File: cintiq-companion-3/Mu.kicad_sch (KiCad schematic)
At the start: 12 parts, among them J1 Conn_01x03_Pin

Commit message: Made a little HSIO plan
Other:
- note added: "I got the flash image tool, so I should be able to change it to whatever I need :3"
- note added: "no actually eDP"
- note added: "rough HSIO plan: HSIO A: idk yet, many possibilities. Could add a B-key m.2 slot with PCIe and USB3 Should probably have at least one Type-A USB3 port too 0: 1: 2: 3: HSIO B: PCIe 4x1, HSIO11 sata/pcie with gpio for M-key m.2 slot 8: SSD PCIe x4 Lane 3 9: SSD PCIe x4 Lane 2 10: SSD PCIe x4 Lane 1 (/ SATA?) 11: SSD PCIe x4 Lane 0 / SATA HSIO C: PCIe 1x1 for E-key m.2 slot for Wifi 6: Wifi PCIe x1"
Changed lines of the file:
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@@
 		)
 	)
-	(text_box "DDI B used for HDMI no actually eDP\n"
+	(text_box "DDI B used for HDMI"
 		(exclude_from_sim no)
 		(at 251.46 231.14 0)
@@
 		)
 	)
-	(text "HSIO functions are defined by the BIOS source code, \nCannot be changed in BIOS settings.\n\nBefore starting design, you should choose one of\nthe available BIOS configurations on:\nhttps://github.com/LattePandaTeam/LattePanda-Mu\nOr contact techsupport for custom your BIOS\n\nThe default functions are defined as follows:\n\n- HSIO0: USB3.2 10Gbps\n- HSIO1: USB3.2 10Gbps\n- HSIO2: PCIe 3.0 x1\n- HSIO3: PCIe 3.0 x1\n\n- HSIO8: PCIe 3.0 x4 (Lane 0)\n- HSIO9: PCIe 3.0 x4 (Lane 1)\n- HSIO10: PCIe 3.0 x4 (Lane 2)\n- HSIO11: PCIe 3.0 x4 (Lane 3)\n\n- HSIO6: PCIe 3.0 x1"
+	(text "HSIO functions are defined by the BIOS source code, \nCannot be changed in BIOS settings.\n\nBefore starting design, you should choose one of\nthe available BIOS configurations on:\nhttps://github.com/LattePandaTeam/LattePanda-Mu\nOr contact techsupport for custom your BIOS\n\nThe default functions are defined as follows:\n\n- HSIO0: USB3.2 10Gbps\n- HSIO1: USB3.2 10Gbps\n- HSIO2: PCIe 3.0 x1\n- HSIO3: PCIe 3.0 x1\n\n- HSIO8: PCIe 3.0 x4 (Lane 0)\n- HSIO9: PCIe 3.0 x4 (Lane 1)\n- HSIO10: PCIe 3.0 x4 (Lane 2)\n- HSIO11: PCIe 3.0 x4 (Lane 3)\n\n- HSIO6: PCIe 3.0 x1\n"
 		(exclude_from_sim no)
-		(at 127 100.33 0)
+		(at 128.27 20.32 0)
 		(effects
 			(font
@@
 		)
 	)
+	(text "no actually eDP\n"
+		(exclude_from_sim no)
+		(at 264.16 237.49 0)
+		(effects
+			(font
+				(size 2.54 2.54)
+				(thickness 0.508)
+				(bold yes)
+				(color 255 121 154 1)
+			)
+			(justify left top)
+		)
+	)
 	(text "HPD pin of unused DDI/TCP port\nneeds to be pulled down"
 		(exclude_from_sim no)
@@
 		)
 	)
+	(text "rough HSIO plan:\n\nHSIO A:\nidk yet, many possibilities.\nCould add a B-key m.2 slot with PCIe and USB3\nShould probably have at least one Type-A USB3 port too\n0:  \n1:  \n2:  \n3:  \n\nHSIO B:\nPCIe 4x1, HSIO11 sata/pcie with gpio for M-key m.2 slot\n8:  SSD PCIe x4 Lane 3\n9:  SSD PCIe x4 Lane 2\n10: SSD PCIe x4 Lane 1 (/ SATA?)\n11: SSD PCIe x4 Lane 0 / SATA\n\nHSIO C:\nPCIe 1x1 for E-key m.2 slot for Wifi\n6:  Wifi PCIe x1 "
+		(exclude_from_sim no)
+		(at 127 123.19 0)
+		(effects
+			(font
+				(size 2.54 2.54)
+				(thickness 0.508)
+				(bold yes)
+				(color 255 121 154 1)
+			)
+			(justify left top)
+		)
+	)
 	(text "DDI/TCP functions are defined by the BIOS source code, \nCannot be changed in BIOS settings.\n\nBefore starting design, you should choose one of\nthe available BIOS configurations on:\nhttps://github.com/LattePandaTeam/LattePanda-Mu\n\nThe default functions are defined as follows:\n\n- DDIA: eDP 1.4b (the 40Pin connector on the Mu)\n\n- DDIB: HDMI 2.0\n\n- TCP0: HDMI 2.0\n\n- TCP1: USB TypeC (need external PD controller)"
 		(exclude_from_sim no)
@@
 		)
 	)
+	(text "I got the flash image tool,\nso I should be able to change\nit to whatever I need :3"
+		(exclude_from_sim no)
+		(at 128.27 107.95 0)
+		(effects
+			(font
+				(size 2.54 2.54)
+				(thickness 0.508)
+				(bold yes)
+				(color 255 121 154 1)
+			)
+			(justify left top)
+		)
+	)
 	(global_label "DDI_B_TX3+"
 		(shape output)
@@
 	)
 	(global_label "TCP0_TXRX0+"
-		(shape output)
+		(shape bidirectional)
 		(at 334.01 285.75 180)
 		(fields_autoplaced yes)
@@
 	)
 	(global_label "TCP0_TXRX1-"
-		(shape output)
+		(shape bidirectional)
 		(at 334.01 278.13 180)
 		(fields_autoplaced yes)
@@
 	)
 	(global_label "eDP_L0-"
-		(shape input)
-		(at 308.61 236.22 180)
-		(fields_autoplaced yes)
-		(effects
-			(font
-				(size 1.27 1.27)
-			)
-			(justify right)
-		)
-		(property "Intersheetrefs" "${INTERSHEET_REFS}"
-			(at 297.2186 236.22 0)
+		(shape output)
+		(at 308.61 255.27 180)
+		(fields_autoplaced yes)
+		(effects
+			(font
+				(size 1.27 1.27)
+			)
+			(justify right)
+		)
+		(property "Intersheetrefs" "${INTERSHEET_REFS}"
+			(at 297.2186 255.27 0)
 			(effects
 				(font
@@
 	)
 	(global_label "TCP1_TXRX0+"
-		(shape output)
+		(shape bidirectional)
 		(at 334.01 323.85 180)
 		(fields_autoplaced yes)
@@
 	)
 	(global_label "TCP0_TXRX0-"
-		(shape output)
+		(shape bidirectional)
 		(at 334.01 288.29 180)
 		(fields_autoplaced yes)
@@
 	)
 	(global_label "eDP_L0+"
-		(shape input)
-		(at 308.61 238.76 180)
-		(fields_autoplaced yes)
-		(effects
-			(font
-				(size 1.27 1.27)
-			)
-			(justify right)
-		)
-		(property "Intersheetrefs" "${INTERSHEET_REFS}"
-			(at 297.2186 238.76 0)
+		(shape output)
+		(at 308.61 252.73 180)
+		(fields_autoplaced yes)
+		(effects
+			(font
+				(size 1.27 1.27)
+			)
+			(justify right)
+		)
+		(property "Intersheetrefs" "${INTERSHEET_REFS}"
+			(at 297.2186 252.73 0)
 			(effects
 				(font
@@
 	)
 	(global_label "eDP_AUX-"
-		(shape input)
-		(at 308.61 246.38 180)
-		(fields_autoplaced yes)
-		(effects
-			(font
-				(size 1.27 1.27)
-			)
-			(justify right)
-		)
-		(property "Intersheetrefs" "${INTERSHEET_REFS}"
-			(at 295.8276 246.38 0)
+		(shape output)
+		(at 308.61 234.95 180)
+		(fields_autoplaced yes)
+		(effects
+			(font
+				(size 1.27 1.27)
+			)
+			(justify right)
+		)
+		(property "Intersheetrefs" "${INTERSHEET_REFS}"
+			(at 295.8276 234.95 0)
 			(effects
 				(font
@@
 	)
 	(global_label "TCP1_TXRX1+"
-		(shape output)
+		(shape bidirectional)
 		(at 334.01 313.69 180)
 		(fields_autoplaced yes)
@@
 	)
 	(global_label "eDP_L1-"
-		(shape input)
-		(at 308.61 228.6 180)
-		(fields_autoplaced yes)
-		(effects
-			(font
-				(size 1.27 1.27)
-			)
-			(justify right)
-		)
-		(property "Intersheetrefs" "${INTERSHEET_REFS}"
-			(at 297.2186 228.6 0)
+		(shape output)
+		(at 308.61 250.19 180)
+		(fields_autoplaced yes)
+		(effects
+			(font
+				(size 1.27 1.27)
+			)
+			(justify right)
+		)
+		(property "Intersheetrefs" "${INTERSHEET_REFS}"
+			(at 297.2186 250.19 0)
 			(effects
 				(font
@@
 	)
 	(global_label "eDP_L1+"
-		(shape input)
-		(at 308.61 231.14 180)
-		(fields_autoplaced yes)
-		(effects
-			(font
-				(size 1.27 1.27)
-			)
-			(justify right)
-		)
-		(property "Intersheetrefs" "${INTERSHEET_REFS}"
-			(at 297.2186 231.14 0)
+		(shape output)
+		(at 308.61 247.65 180)
+		(fields_autoplaced yes)
+		(effects
+			(font
+				(size 1.27 1.27)
+			)
+			(justify right)
+		)
+		(property "Intersheetrefs" "${INTERSHEET_REFS}"
+			(at 297.2186 247.65 0)
 			(effects
 				(font
@@
 	(global_label "eDP_HPD"
 		(shape input)
-		(at 308.61 251.46 180)
-		(fields_autoplaced yes)
-		(effects
-			(font
-				(size 1.27 1.27)
-			)
-			(justify right)
-		)
-		(property "Intersheetrefs" "${INTERSHEET_REFS}"
-			(at 297.1581 251.46 0)
+		(at 308.61 222.25 180)
+		(fields_autoplaced yes)
+		(effects
+			(font
+				(size 1.27 1.27)
+			)
+			(justify right)
+		)
+		(property "Intersheetrefs" "${INTERSHEET_REFS}"
+			(at 297.1581 222.25 0)
 			(effects
 				(font
@@
 	)
 	(global_label "TCP1_TXRX1-"
-		(shape output)
+		(shape bidirectional)
 		(at 334.01 316.23 180)
 		(fields_autoplaced yes)
@@
 	)
 	(global_label "TCP0_TXRX1+"
-		(shape output)
+		(shape bidirectional)
 		(at 334.01 275.59 180)
 		(fields_autoplaced yes)
@@
 	)
 	(global_label "TCP1_TXRX0-"
-		(shape output)
+		(shape bidirectional)
 		(at 334.01 326.39 180)
 		(fields_autoplaced yes)
@@
 	)
 	(global_label "eDP_AUX+"
-		(shape input)
-		(at 308.61 243.84 180)
-		(fields_autoplaced yes)
-		(effects
-			(font
-				(size 1.27 1.27)
-			)
-			(justify right)
-		)
-		(property "Intersheetrefs" "${INTERSHEET_REFS}"
-			(at 295.8276 243.84 0)
-			(effects
-				(font
+		(shape output)
+		(at 308.61 232.41 180)
+		(fields_autoplaced yes)
+		(effects
+			(font
+				(size 1.27 1.27)
+			)
+			(justify right)
+		)
+		(property "Intersheetrefs" "${INTERSHEET_REFS}"
+			(at 295.8276 232.41 0)
+			(effects
+				(font

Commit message: Did some footprint assignments and added reference image to pcb editor
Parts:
- A1: footprint Module_LattePanda:LattePanda_Module_H8.0mm_Horizontal -> A_my_stuff:ddr4sodimm
- H7, H8: footprint A_HDJ_Library:MountingHole_3mm_M2_Pad_TopOnly -> MountingHole:MountingHole_3mm_Pad_TopOnly
- J1: footprint A_HDJ_Library:PinHeader_1x03_P2.54mm_Vertical -> Connector_PinHeader_2.54mm:PinHeader_1x03_P2.54mm_Vertical
- R4, R5, R6, R7: footprint A_HDJ_Library:R_0402_1005Metric -> Resistor_SMD:R_0402_1005Metric
- TP2: footprint A_HDJ_Library:TestPoint_Pad_D1.5mm -> TestPoint:TestPoint_Pad_D1.5mm
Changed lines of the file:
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@@
 			)
 		)
-		(property "Footprint" "A_HDJ_Library:R_0402_1005Metric"
+		(property "Footprint" "Resistor_SMD:R_0402_1005Metric"
 			(at 278.13 258.572 90)
 			(effects
@@
 			)
 		)
-		(property "Footprint" "A_HDJ_Library:R_0402_1005Metric"
+		(property "Footprint" "Resistor_SMD:R_0402_1005Metric"
 			(at 278.13 296.672 90)
 			(effects
@@
 			)
 		)
-		(property "Footprint" "Module_LattePanda:LattePanda_Module_H8.0mm_Horizontal"
+		(property "Footprint" "A_my_stuff:ddr4sodimm"
 			(at 294.386 179.07 0)
 			(effects
@@
 			)
 		)
-		(property "Footprint" "A_HDJ_Library:MountingHole_3mm_M2_Pad_TopOnly"
+		(property "Footprint" "MountingHole:MountingHole_3mm_Pad_TopOnly"
 			(at 515.62 311.15 0)
 			(effects
@@
 			)
 		)
-		(property "Footprint" "A_HDJ_Library:R_0402_1005Metric"
+		(property "Footprint" "Resistor_SMD:R_0402_1005Metric"
 			(at 412.75 57.658 90)
 			(effects
@@
 			)
 		)
-		(property "Footprint" "A_HDJ_Library:R_0402_1005Metric"
+		(property "Footprint" "Resistor_SMD:R_0402_1005Metric"
 			(at 438.15 269.748 90)
 			(effects
@@
 			)
 		)
-		(property "Footprint" "A_HDJ_Library:TestPoint_Pad_D1.5mm"
+		(property "Footprint" "TestPoint:TestPoint_Pad_D1.5mm"
 			(at 436.88 267.97 0)
 			(effects
@@
 			)
 		)
-		(property "Footprint" "A_HDJ_Library:MountingHole_3mm_M2_Pad_TopOnly"
+		(property "Footprint" "MountingHole:MountingHole_3mm_Pad_TopOnly"
 			(at 490.22 311.15 0)
 			(effects
@@
 			)
 		)
-		(property "Footprint" "A_HDJ_Library:PinHeader_1x03_P2.54mm_Vertical"
+		(property "Footprint" "Connector_PinHeader_2.54mm:PinHeader_1x03_P2.54mm_Vertical"
 			(at 292.1 74.93 0)
 			(effects

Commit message: Redid board outline according to reference and placed compute module slot
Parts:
- A1: footprint A_my_stuff:ddr4sodimm -> A_my_stuff:LattepandaMuFlat
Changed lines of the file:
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@@
 			)
 		)
-		(property "Footprint" "A_my_stuff:ddr4sodimm"
+		(property "Footprint" "A_my_stuff:LattepandaMuFlat"
 			(at 294.386 179.07 0)
 			(effects

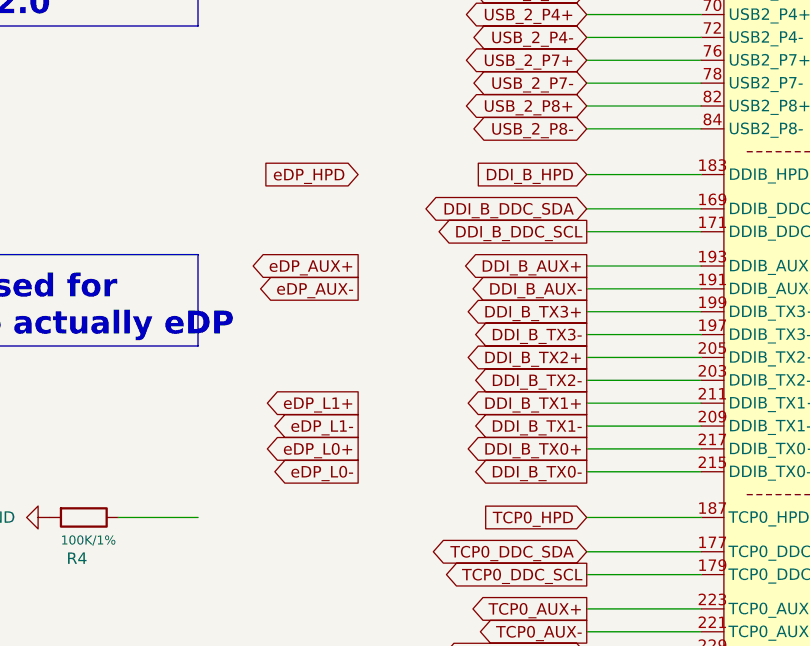
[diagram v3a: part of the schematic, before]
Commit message: Added m.2 ssd slot, did some test routing
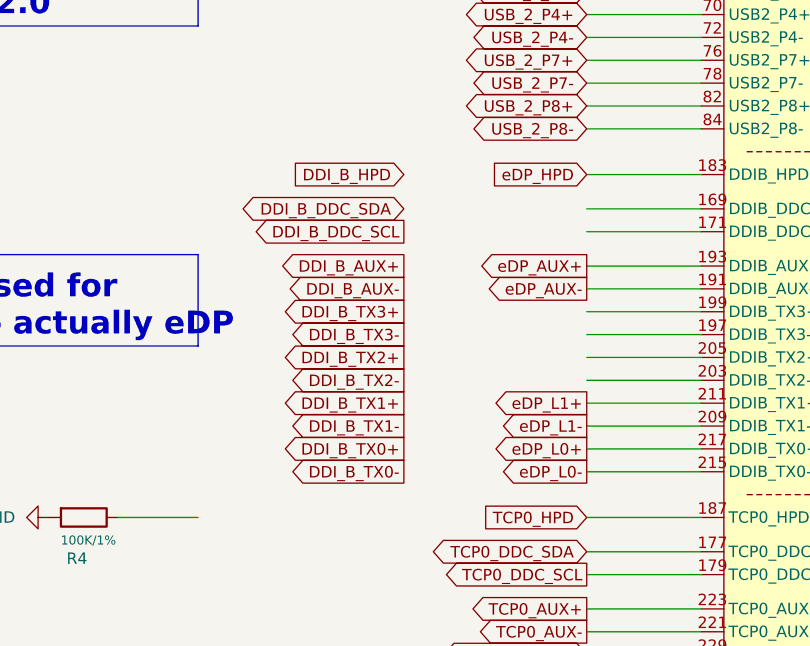
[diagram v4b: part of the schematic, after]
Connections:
- net DDI_B_AUX+: no longer A1.193 (DDIB_AUX+)
- net DDI_B_AUX-: no longer A1.191 (DDIB_AUX-)
- net DDI_B_DDC_SCL: no longer A1.171 (DDIB_DDC_SCL)
- net DDI_B_DDC_SDA: no longer A1.169 (DDIB_DDC_SDA)
- net DDI_B_HPD: no longer A1.183 (DDIB_HPD)
- net DDI_B_TX0+: no longer A1.217 (DDIB_TX0+)
- net DDI_B_TX0-: no longer A1.215 (DDIB_TX0-)
- net DDI_B_TX1+: no longer A1.211 (DDIB_TX1+)
- net DDI_B_TX1-: no longer A1.209 (DDIB_TX1-)
- net DDI_B_TX2+: no longer A1.205 (DDIB_TX2+)
- net DDI_B_TX2-: no longer A1.203 (DDIB_TX2-)
- net DDI_B_TX3+: no longer A1.199 (DDIB_TX3+)
- net DDI_B_TX3-: no longer A1.197 (DDIB_TX3-)
- net eDP_AUX+: now also A1.193 (DDIB_AUX+)
- net eDP_AUX-: now also A1.191 (DDIB_AUX-)
- net eDP_HPD: now also A1.183 (DDIB_HPD)
- net eDP_L0+: now also A1.217 (DDIB_TX0+)
- net eDP_L0-: now also A1.215 (DDIB_TX0-)
- net eDP_L1+: now also A1.211 (DDIB_TX1+)
- net eDP_L1-: now also A1.209 (DDIB_TX1-)
